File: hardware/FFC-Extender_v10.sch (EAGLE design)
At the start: 6 parts, among them J1 FPC40, J2 FPC40, X1 PASSER, X2 PASSER, X3 PASSER, X4 PASSER

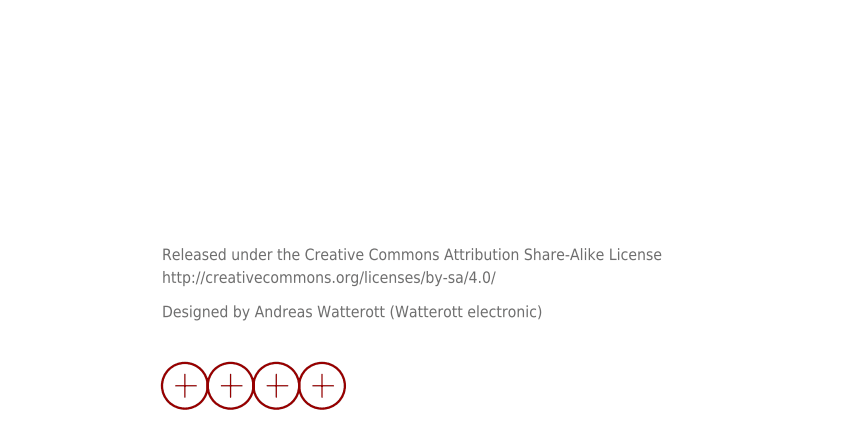
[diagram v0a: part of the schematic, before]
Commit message: updated schematics
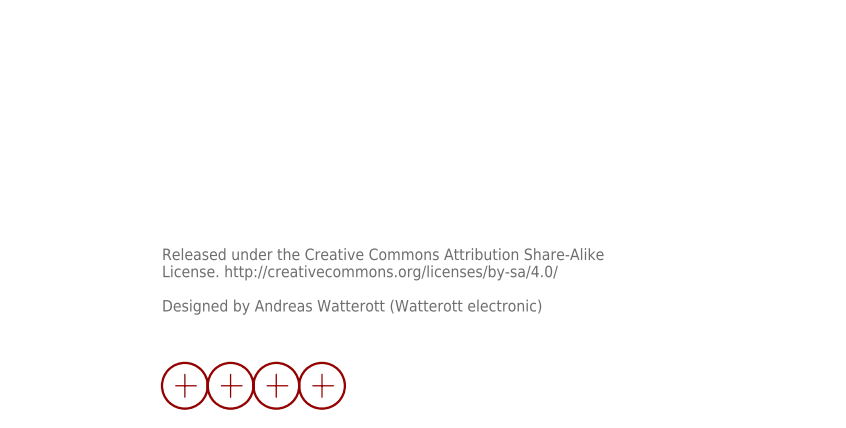
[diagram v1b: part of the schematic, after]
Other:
- note added: "Released under the Creative Commons Attribution Share-Alike License. http://creativecommons.org/licenses/by-sa/4.0/ Designed by Andreas Watterott (Watterott electronic)"
- note removed: "Designed by Andreas Watterott (Watterott electronic)"
- note removed: "Released under the Creative Commons Attribution Share-Alike License"
- note removed: "http://creativecommons.org/licenses/by-sa/4.0/"
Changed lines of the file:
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@@
 <?xml version="1.0" encoding="utf-8"?>
 <!DOCTYPE eagle SYSTEM "eagle.dtd">
-<eagle version="7.3.0">
+<eagle version="7.5.0">
 <drawing>
 <settings>
@@
 <setting verticaltext="up"/>
 </settings>
-<grid distance="0.1" unitdist="inch" unit="inch" style="lines" multiple="1" display="no" altdistance="0.01" altunitdist="inch" altunit="inch"/>
+<grid distance="0.05" unitdist="inch" unit="inch" style="lines" multiple="1" display="yes" altdistance="0.025" altunitdist="inch" altunit="inch"/>
 <layers>
 <layer number="1" name="Top" color="4" fill="1" visible="no" active="no"/>
@@
 <layer number="51" name="tDocu" color="7" fill="1" visible="no" active="no"/>
 <layer number="52" name="bDocu" color="7" fill="1" visible="no" active="no"/>
-<layer number="53" name="tCopper" color="7" fill="11" visible="no" active="no"/>
-<layer number="54" name="bCopper" color="7" fill="1" visible="no" active="no"/>
-<layer number="56" name="wert" color="7" fill="1" visible="no" active="no"/>
-<layer number="57" name="tCAD" color="7" fill="1" visible="no" active="no"/>
 <layer number="91" name="Nets" color="2" fill="1" visible="yes" active="yes"/>
 <layer number="92" name="Busses" color="1" fill="1" visible="yes" active="yes"/>
@@
 <layer number="98" name="Guide" color="6" fill="1" visible="yes" active="yes"/>
 <layer number="99" name="SpiceOrder" color="5" fill="1" visible="yes" active="yes"/>
-<layer number="100" name="Muster" color="7" fill="1" visible="no" active="no"/>
-<layer number="153" name="FabDoc1" color="6" fill="1" visible="no" active="no"/>
-<layer number="154" name="FabDoc2" color="2" fill="1" visible="no" active="no"/>
-<layer number="155" name="FabDoc3" color="7" fill="15" visible="no" active="no"/>
-<layer number="217" name="217bmp" color="18" fill="1" visible="no" active="no"/>
-<layer number="218" name="218bmp" color="19" fill="1" visible="no" active="no"/>
-<layer number="219" name="219bmp" color="20" fill="1" visible="no" active="no"/>
-<layer number="220" name="220bmp" color="21" fill="1" visible="no" active="no"/>
-<layer number="221" name="221bmp" color="22" fill="1" visible="no" active="no"/>
-<layer number="222" name="222bmp" color="23" fill="1" visible="no" active="no"/>
-<layer number="223" name="223bmp" color="24" fill="1" visible="no" active="no"/>
-<layer number="224" name="224bmp" color="25" fill="1" visible="no" active="no"/>
-<layer number="251" name="SMDround" color="12" fill="11" visible="no" active="no"/>
 </layers>
 <schematic xreflabel="%F%N/%S.%C%R" xrefpart="/%S.%C%R">
@@
 <sheet>
 <plain>
-<text x="162.56" y="21.59" size="1.27" layer="95">Released under the Creative Commons Attribution Share-Alike License</text>
-<text x="162.56" y="19.05" size="1.27" layer="95">http://creativecommons.org/licenses/by-sa/4.0/</text>
-<text x="162.56" y="15.24" size="1.27" layer="95">Designed by Andreas Watterott (Watterott electronic)</text>
+<text x="162.56" y="22.86" size="1.27" layer="95" align="top-left">Released under the Creative Commons Attribution Share-Alike
+License. http://creativecommons.org/licenses/by-sa/4.0/
+Designed by Andreas Watterott (Watterott electronic)</text>
 </plain>
 <instances>
@@
 </schematic>
 </drawing>
+<compatibility>
+<note version="6.3" minversion="6.2.2" severity="warning">
+Since Version 6.2.2 text objects can contain more than one line,
+which will not be processed correctly with this version.
+</note>
+</compatibility>
 </eagle>
